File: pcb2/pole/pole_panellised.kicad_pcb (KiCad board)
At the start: 2 copper layers, 49 x 39 mm, 100 parts, among them IC1 LMx93, IC2 STM32F0xxKxUx, P1 POWER_IN, P2 BUS_IN, P3 BUS_OUT, P4 SWD_TC, P5 LEDs, Q1 MTM232270LBF, Q2 MTM232270LBF, Q3 MTM232270LBF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

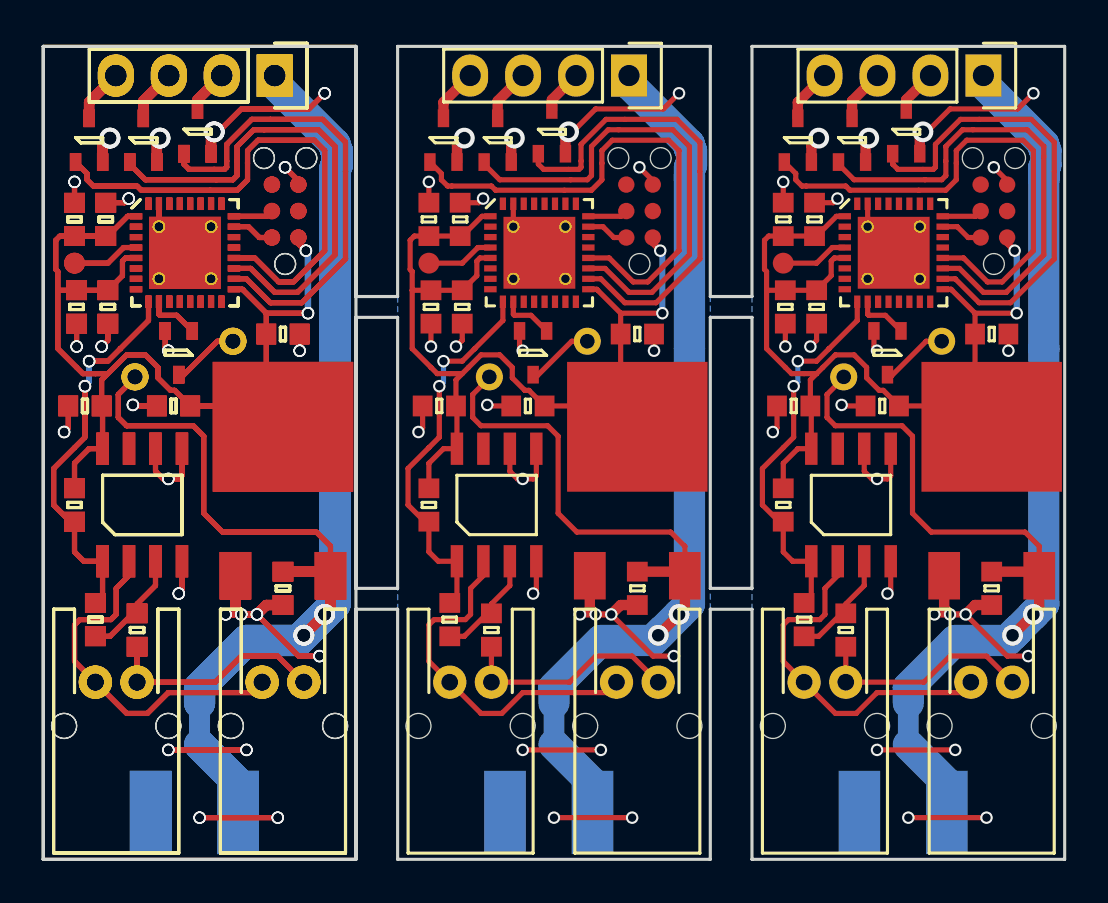
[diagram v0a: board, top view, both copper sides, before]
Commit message: Changed vias from 0.6/0.4 to 0.6/0.3
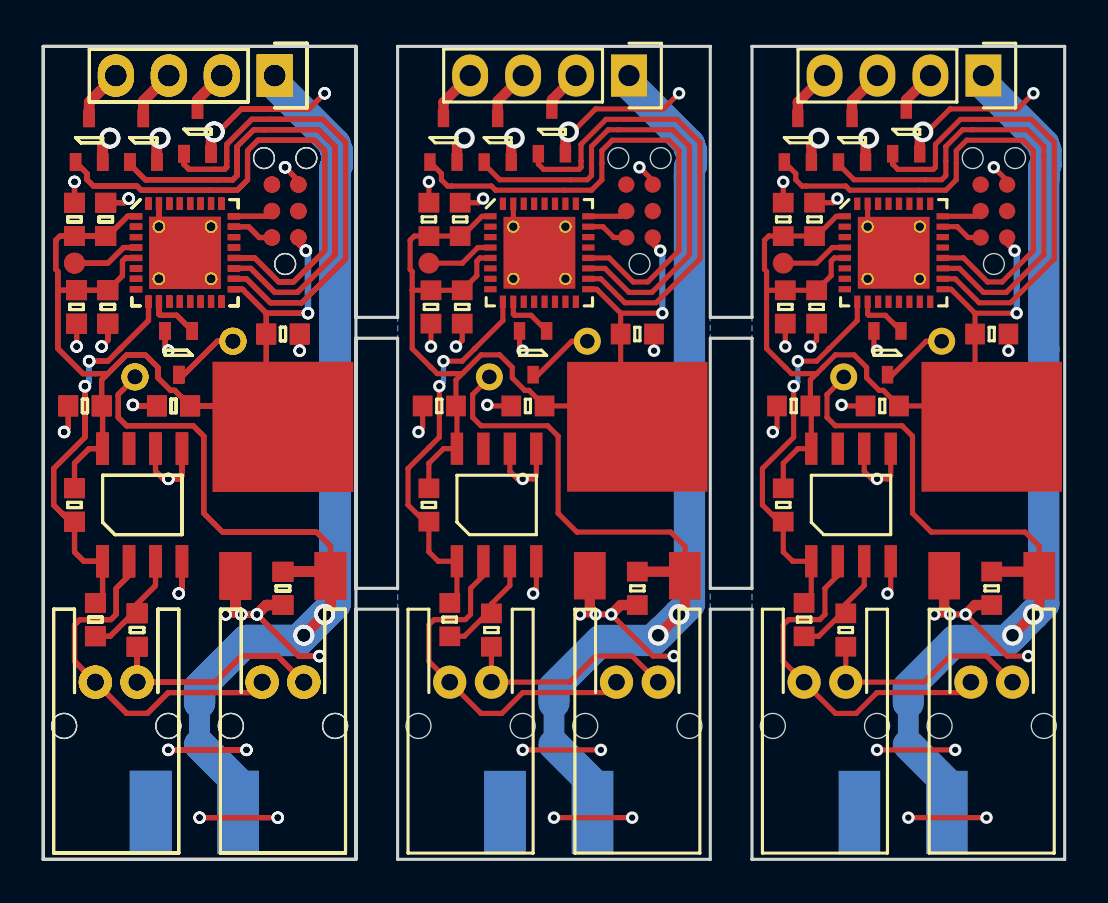
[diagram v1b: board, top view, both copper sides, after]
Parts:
- removed the C1 at (118.0, 93.2) (x2)
- removed the C2 at (117.5, 84.3) (x2)
- removed the C3 at (119.0, 84.3) (x2)
- removed the C4 at (119.1, 88.5) (x2)
- removed the C5 at (127.5, 89.8) (x2)
- removed the C6 at (127.5, 102.0) (x2)
- removed the C7 at (122.2, 93.2) (x2)
- removed the C8 at (117.6, 88.5) (x2)
- removed the IC1 at (120.8, 98.0) (x2)
- removed the IC2 at (122.8, 85.9) (x2)
- removed the P1 at (123.2, 114.8) (x2)
- removed the P2 at (119.5, 106.5) (x2)
- removed the P3 at (127.5, 106.5) (x2)
- removed the P4 at (127.6, 83.9) (x2)
- removed the P5 at (127.1, 77.4) (x2)
- removed the Q1 at (123.4, 80.1) (x2)
- removed the Q2 at (120.8, 80.5) (x2)
- removed the Q3 at (118.2, 80.5) (x2)
- removed the Q4 at (122.5, 90.7) (x2)
- removed the R1 at (117.5, 98.0) (x2)
- removed the R2 at (120.5, 104.0) (x2)
- removed the R3 at (118.5, 103.5) (x2)
- removed the SP1 at (122.8, 91.0) (x2)
- removed the TP1 at (117.5, 86.4) (x2)
- removed the U1 at (127.5, 94.2) (x2)
- added C1 (x2): 100n, agg:0603, F.Cu at (118.0, 93.2)
- added C2 (x2): 4u7, agg:0603, F.Cu at (117.5, 84.3)
- added C3 (x2): 100n, agg:0603, F.Cu at (119.0, 84.3)
- added C4 (x2): 10n, agg:0603, F.Cu at (119.1, 88.5)
- added C5 (x2): 100n, agg:0603, F.Cu at (127.5, 89.8)
- added C6 (x2): 100n, agg:0603, F.Cu at (127.5, 102.0)
- added C7 (x2): 10u, agg:0603, F.Cu at (122.2, 93.2)
- added C8 (x2): 1u, agg:0603, F.Cu at (117.6, 88.5)
- added IC1 (x2): LMx93, SOIC-8, F.Cu at (120.8, 98.0)
- added IC2 (x2): STM32F0xxKxUx, agg:QFN-32-EP-ST, F.Cu at (122.8, 85.9)
- added P1 (x2): POWER_IN, thegrid:minipow_edge, B.Cu at (123.2, 114.8)
- added P2 (x2): BUS_IN, agg:S02B-PASK-2, F.Cu at (119.5, 106.5)
- added P3 (x2): BUS_OUT, agg:S02B-PASK-2, F.Cu at (127.5, 106.5)
- added P4 (x2): SWD_TC, agg:TC2030-NL, F.Cu at (127.6, 83.9)
- added P5 (x2): LEDs, Pin_Headers:Pin_Header_Straight_1x04, F.Cu at (127.1, 77.4)
- added Q1 (x2): MTM232270LBF, agg:SOT-323, F.Cu at (123.4, 80.1)
- added Q2 (x2): MTM232270LBF, agg:SOT-323, F.Cu at (120.8, 80.5)
- added Q3 (x2): MTM232270LBF, agg:SOT-323, F.Cu at (118.2, 80.5)
- added Q4 (x2): MTM232270LBF, agg:SOT-323, F.Cu at (122.5, 90.7)
- added R1 (x2): 10k, agg:0603, F.Cu at (117.5, 98.0)
- added R2 (x2): 10k, agg:0603, F.Cu at (120.5, 104.0)
- added R3 (x2): 1M, agg:0603, F.Cu at (118.5, 103.5)
- added SP1 (x2): SPEAKER, thegrid:piezo, B.Cu at (122.8, 91.0)
- added TP1 (x2): RST, agg:TESTPAD, F.Cu at (117.5, 86.4)
- added U1 (x2): LD1117S33TR, thegrid:TO-252-3, F.Cu at (127.5, 94.2)
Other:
- outline, holes or cut-outs redrawn

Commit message: Removed erroneous edge cut
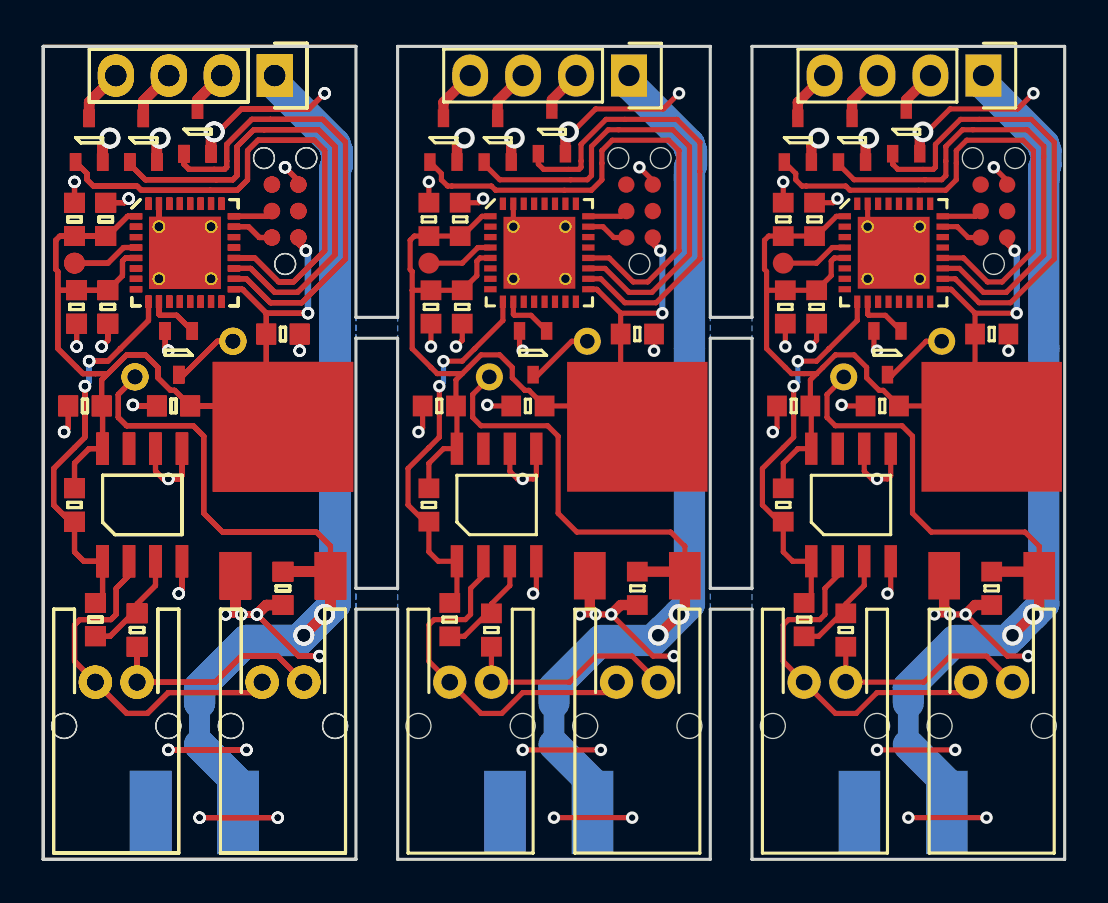
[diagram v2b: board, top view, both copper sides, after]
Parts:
- removed the C1 at (118.0, 93.2) (x2)
- removed the C2 at (117.5, 84.3) (x2)
- removed the C3 at (119.0, 84.3) (x2)
- removed the C4 at (119.1, 88.5) (x2)
- removed the C5 at (127.5, 89.8) (x2)
- removed the C6 at (127.5, 102.0) (x2)
- removed the C7 at (122.2, 93.2) (x2)
- removed the C8 at (117.6, 88.5) (x2)
- removed the IC1 at (120.8, 98.0) (x2)
- removed the IC2 at (122.8, 85.9) (x2)
- removed the P1 at (123.2, 114.8) (x2)
- removed the P2 at (119.5, 106.5) (x2)
- removed the P3 at (127.5, 106.5) (x2)
- removed the P4 at (127.6, 83.9) (x2)
- removed the P5 at (127.1, 77.4) (x2)
- removed the Q1 at (123.4, 80.1) (x2)
- removed the Q2 at (120.8, 80.5) (x2)
- removed the Q3 at (118.2, 80.5) (x2)
- removed the Q4 at (122.5, 90.7) (x2)
- removed the R1 at (117.5, 98.0) (x2)
- removed the R2 at (120.5, 104.0) (x2)
- removed the R3 at (118.5, 103.5) (x2)
- removed the SP1 at (122.8, 91.0) (x2)
- removed the TP1 at (117.5, 86.4) (x2)
- removed the U1 at (127.5, 94.2) (x2)
- added C1 (x2): 100n, agg:0603, F.Cu at (118.0, 93.2)
- added C2 (x2): 4u7, agg:0603, F.Cu at (117.5, 84.3)
- added C3 (x2): 100n, agg:0603, F.Cu at (119.0, 84.3)
- added C4 (x2): 10n, agg:0603, F.Cu at (119.1, 88.5)
- added C5 (x2): 100n, agg:0603, F.Cu at (127.5, 89.8)
- added C6 (x2): 100n, agg:0603, F.Cu at (127.5, 102.0)
- added C7 (x2): 10u, agg:0603, F.Cu at (122.2, 93.2)
- added C8 (x2): 1u, agg:0603, F.Cu at (117.6, 88.5)
- added IC1 (x2): LMx93, SOIC-8, F.Cu at (120.8, 98.0)
- added IC2 (x2): STM32F0xxKxUx, agg:QFN-32-EP-ST, F.Cu at (122.8, 85.9)
- added P1 (x2): POWER_IN, thegrid:minipow_edge, B.Cu at (123.2, 114.8)
- added P2 (x2): BUS_IN, agg:S02B-PASK-2, F.Cu at (119.5, 106.5)
- added P3 (x2): BUS_OUT, agg:S02B-PASK-2, F.Cu at (127.5, 106.5)
- added P4 (x2): SWD_TC, agg:TC2030-NL, F.Cu at (127.6, 83.9)
- added P5 (x2): LEDs, Pin_Headers:Pin_Header_Straight_1x04, F.Cu at (127.1, 77.4)
- added Q1 (x2): MTM232270LBF, agg:SOT-323, F.Cu at (123.4, 80.1)
- added Q2 (x2): MTM232270LBF, agg:SOT-323, F.Cu at (120.8, 80.5)
- added Q3 (x2): MTM232270LBF, agg:SOT-323, F.Cu at (118.2, 80.5)
- added Q4 (x2): MTM232270LBF, agg:SOT-323, F.Cu at (122.5, 90.7)
- added R1 (x2): 10k, agg:0603, F.Cu at (117.5, 98.0)
- added R2 (x2): 10k, agg:0603, F.Cu at (120.5, 104.0)
- added R3 (x2): 1M, agg:0603, F.Cu at (118.5, 103.5)
- added SP1 (x2): SPEAKER, thegrid:piezo, B.Cu at (122.8, 91.0)
- added TP1 (x2): RST, agg:TESTPAD, F.Cu at (117.5, 86.4)
- added U1 (x2): LD1117S33TR, thegrid:TO-252-3, F.Cu at (127.5, 94.2)
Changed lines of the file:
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@@
     (area 114.7 74.160714 167.125 127.975001)
     (thickness 1.6)
-    (drawings 48)
+    (drawings 47)
     (tracks 1144)
     (zones 0)
@@
     (effects (font (size 1.5 1.5) (thickness 0.3)) (justify mirror))
   )
-  (gr_line (start 131 115) (end 131 76) (angle 90) (layer Edge.Cuts) (width 0.15))
   (gr_line (start 116 76) (end 116 115) (angle 90) (layer Edge.Cuts) (width 0.15))
   (gr_line (start 116 76) (end 131 76) (angle 90) (layer Edge.Cuts) (width 0.15))
